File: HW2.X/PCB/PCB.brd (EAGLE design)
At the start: 50 x 50 mm, 22 parts

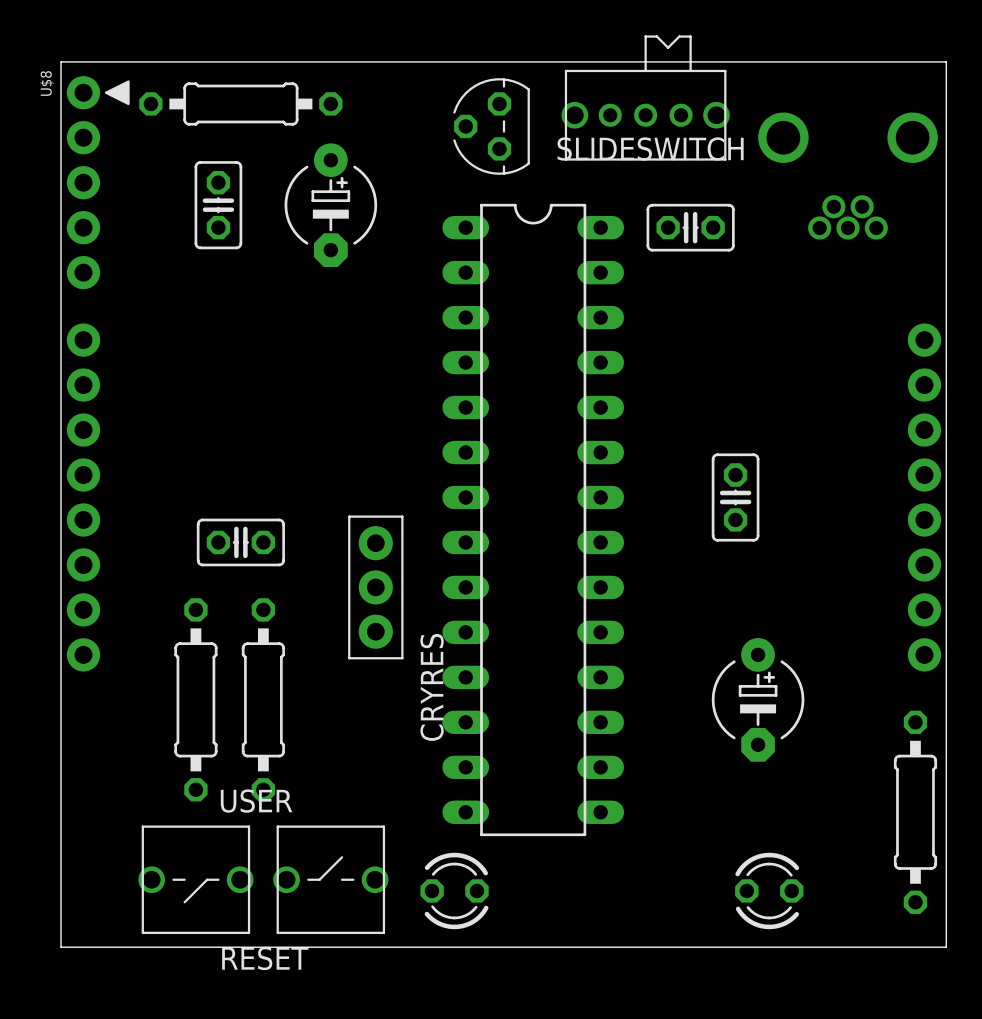
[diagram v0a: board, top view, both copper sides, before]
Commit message: PCB Fix component positions
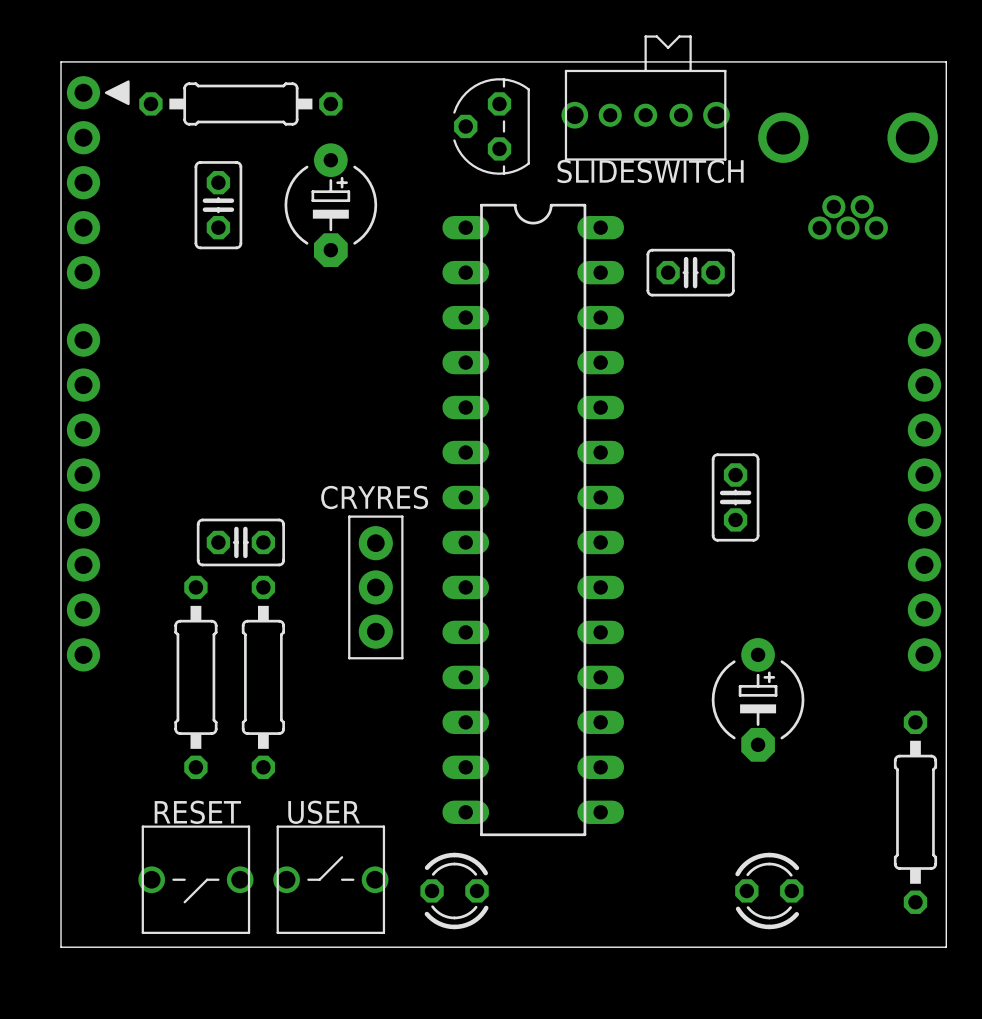
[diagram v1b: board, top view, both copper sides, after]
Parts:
- moved C2 2.54 mm to (35.6, 38.1)
- moved R2 1.27 mm to (11.4, 15.2)
- moved R4 1.27 mm to (7.62, 15.2)
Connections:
- net N$10 renamed PEGD1
- net N$11 renamed PEGC1
- net N$18 renamed VCAP
- net N$3 renamed MCLR
- net N$4 renamed OSC1
- net N$5 renamed OSC2
- net N$7 renamed D-
- net N$8 renamed D+
- net N$9 renamed USBID

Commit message: PCB Update
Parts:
- turned USER to 180 degrees
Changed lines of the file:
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@@
 <attribute name="VALUE" x="3.048" y="44.45" size="1.27" layer="27" ratio="20" rot="R270"/>
 </element>
-<element name="USER" library="ME433" package="SWITCH" value="SWITCH" x="15.24" y="3.81" smashed="yes">
-<attribute name="NAME" x="12.7" y="6.985" size="1.27" layer="21"/>
+<element name="USER" library="ME433" package="SWITCH" value="SWITCH" x="15.24" y="3.81" smashed="yes" rot="R180">
+<attribute name="NAME" x="17.145" y="8.255" size="1.27" layer="21" rot="R180"/>
 </element>
 </elements>
@@
 <wire x1="7.62" y1="10.16" x2="1.27" y2="16.51" width="0" layer="19" extent="1-1"/>
 <wire x1="5.12" y1="3.81" x2="7.62" y2="10.16" width="0" layer="19" extent="1-1"/>
-<wire x1="17.74" y1="3.81" x2="7.62" y2="10.16" width="0" layer="19" extent="1-1"/>
+<wire x1="12.74" y1="3.81" x2="7.62" y2="10.16" width="0" layer="19" extent="1-1"/>
 </signal>
 <signal name="N$1">
@@
 <contactref element="USER" pad="2"/>
 <wire x1="11.43" y1="10.16" x2="22.86" y2="15.24" width="0" layer="19" extent="1-1"/>
-<wire x1="12.74" y1="3.81" x2="11.43" y2="10.16" width="0" layer="19" extent="1-1"/>
+<wire x1="17.74" y1="3.81" x2="11.43" y2="10.16" width="0" layer="19" extent="1-1"/>
 <wire x1="1.27" y1="24.13" x2="11.43" y2="10.16" width="0" layer="19" extent="1-1"/>
 </signal>
